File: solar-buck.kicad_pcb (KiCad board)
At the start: 2 copper layers, 51 parts, among them J1 PV_input, J2 Conn_02x19_Odd_Even, J3 Conn_02x19_Odd_Even, J4 Load_output, J5 Batt_output, J6 LED_ON, Q1 PMN30ENEA, Q2 PMN30ENEA, Q3 NX3008PBK, Q4 NX3008PBK, SW1 SW_Push, SW2 SW_Push, SW3 SW_Push, SW4 SW_Push, U1 TS2937, U2 MAX1614, U3 MCP1804, U4 L6285E, U5 MAX4378

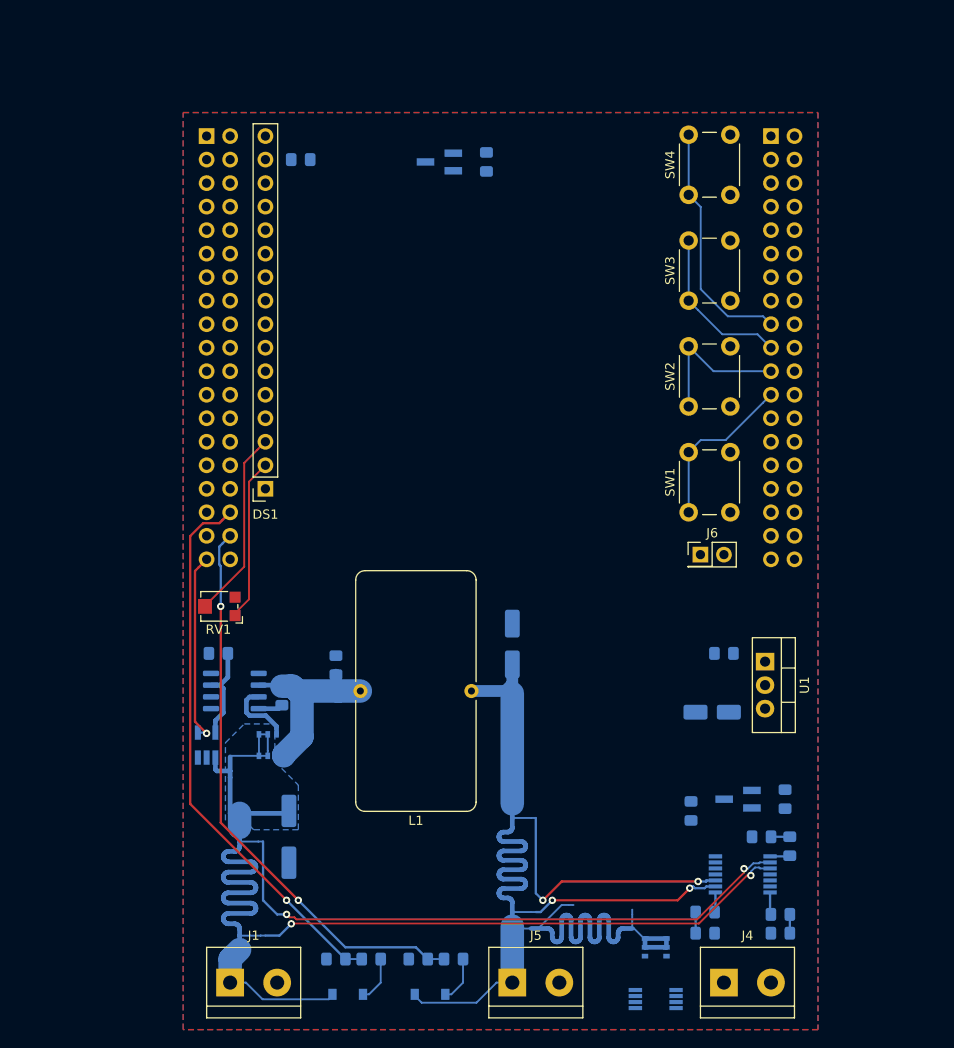
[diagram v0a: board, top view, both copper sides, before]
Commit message: Updated PCB footprints
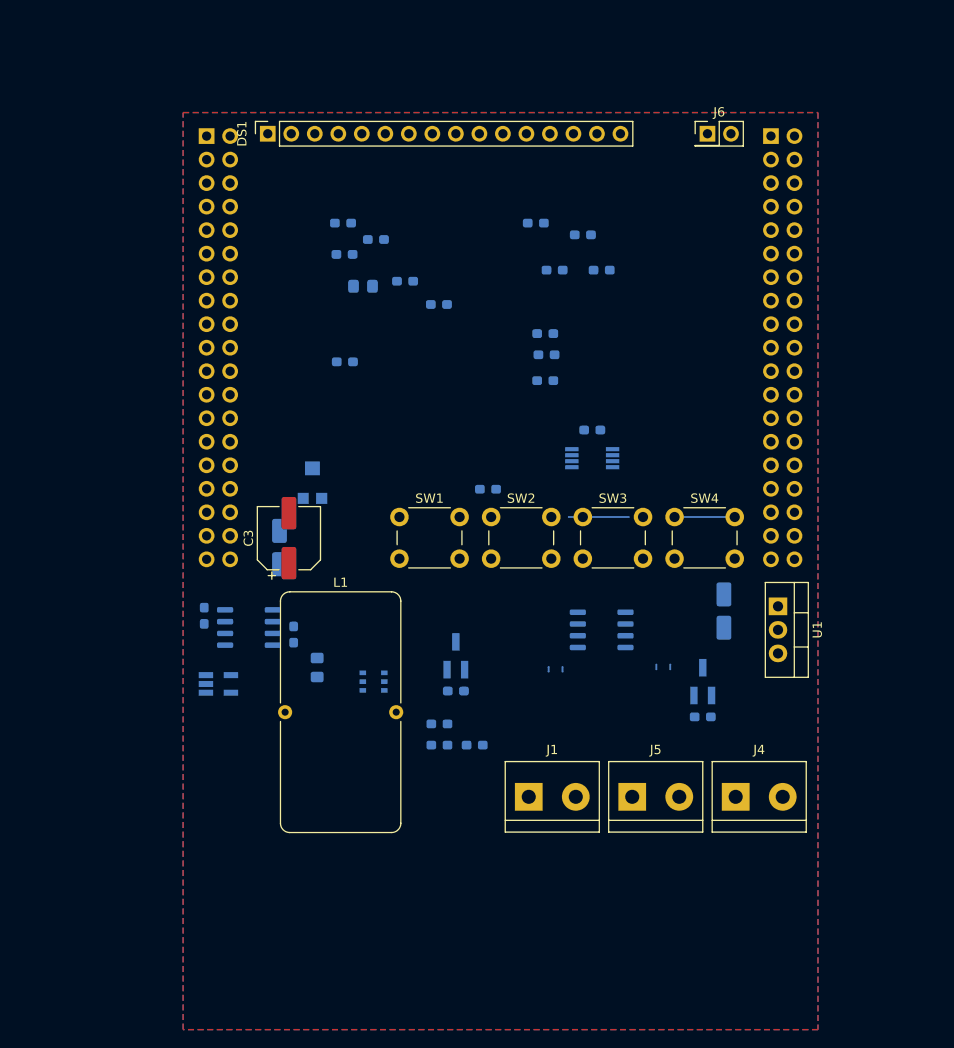
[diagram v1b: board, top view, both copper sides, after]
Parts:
- removed D2: MMSZ5237BT1G, Diode_SMD:D_SOD-123
- removed D3: MMSZ5243BT1G, Diode_SMD:D_SOD-123
- removed NT3, NT4: Net-Tie_2, local:NetTie-2_SMD_Pad8mil
- removed Q1: PMN30ENEA, Package_SO:TSOP-6_1.65x3.05mm_P0.95mm
- added C11: 100n, Capacitor_SMD:C_0603_1608Metric_Pad1.05x0.95mm_HandSolder, B.Cu at (178.3, 69.6)
- added D4: RBR5LAM-30TR, Diode_SMD:D_0805_2012Metric_Pad1.15x1.40mm_HandSolder, B.Cu at (176.9, 74.6)
- added R11: 10k, Resistor_SMD:R_0603_1608Metric_Pad1.05x0.95mm_HandSolder, B.Cu at (181.5, 74.1)
- added R12: 100, Resistor_SMD:R_0603_1608Metric_Pad1.05x0.95mm_HandSolder, B.Cu at (185.2, 124.2)
- added R13: 10k, Resistor_SMD:R_0603_1608Metric_Pad1.05x0.95mm_HandSolder, B.Cu at (185.2, 121.9)
- added R14: 100, Resistor_SMD:R_0603_1608Metric_Pad1.05x0.95mm_HandSolder, B.Cu at (189.0, 124.2)
- C10, C2, C4, C5, C7, C8, C9: footprint Capacitor_SMD:C_0805_2012Metric_Pad1.15x1.40mm_HandSolder -> Capacitor_SMD:C_0603_1608Metric_Pad1.05x0.95mm_HandSolder
- C3: footprint Capacitor_SMD:CP_Elec_6.3x5.4 -> Capacitor_SMD:CP_Elec_6.3x7.7; moved to F.Cu
- C6: footprint Capacitor_SMD:CP_Elec_5x5.4 -> Capacitor_SMD:CP_Elec_4x5.4
- R1, R3: value 10k -> 200k; footprint Resistor_SMD:R_0805_2012Metric_Pad1.15x1.40mm_HandSolder -> Resistor_SMD:R_0603_1608Metric_Pad1.05x0.95mm_HandSolder
- R10: value 100k -> 200k; footprint Resistor_SMD:R_0805_2012Metric_Pad1.15x1.40mm_HandSolder -> Resistor_SMD:R_0603_1608Metric_Pad1.05x0.95mm_HandSolder
- R2: value 200 -> 100; footprint Resistor_SMD:R_0805_2012Metric_Pad1.15x1.40mm_HandSolder -> Resistor_SMD:R_0603_1608Metric_Pad1.05x0.95mm_HandSolder
- R4: value 150k -> 1.8M; footprint Resistor_SMD:R_0805_2012Metric_Pad1.15x1.40mm_HandSolder -> Resistor_SMD:R_0603_1608Metric_Pad1.05x0.95mm_HandSolder
- R5: value 200k -> 1.8M; footprint Resistor_SMD:R_0805_2012Metric_Pad1.15x1.40mm_HandSolder -> Resistor_SMD:R_0603_1608Metric_Pad1.05x0.95mm_HandSolder
- R6, R8: footprint Resistor_SMD:R_0805_2012Metric_Pad1.15x1.40mm_HandSolder -> Resistor_SMD:R_0603_1608Metric_Pad1.05x0.95mm_HandSolder
- R7: value 3.3k -> 10k; footprint Resistor_SMD:R_0805_2012Metric_Pad1.15x1.40mm_HandSolder -> Resistor_SMD:R_0603_1608Metric_Pad1.05x0.95mm_HandSolder
- R9: value 120k -> 200k; footprint Resistor_SMD:R_0805_2012Metric_Pad1.15x1.40mm_HandSolder -> Resistor_SMD:R_0603_1608Metric_Pad1.05x0.95mm_HandSolder
- RV1: moved to B.Cu
- U2: value MAX1614 -> VN5E160MS-E; footprint Package_SO:MSOP-8_3x3mm_P0.65mm -> Package_SO:SO-8_3.9x4.9mm_P1.27mm
- U5: value MAX4378 -> MAX4377; footprint Package_SO:TSSOP-14_4.4x5mm_P0.65mm -> Package_SO:MSOP-8_3x3mm_P0.65mm
- moved R10 79.5 mm to (174.8, 67.8)
- moved R8 76.6 mm to (195.6, 67.8)
- moved R5 76.2 mm to (174.9, 71.2)
- moved R7 75.5 mm to (185.1, 76.6), turned to 0 degrees
- moved C10 73.4 mm to (197.6, 72.9), turned to 0 degrees
- moved R9 68.9 mm to (196.6, 79.8)
- moved C8 67.8 mm to (200.7, 69.1), turned to 0 degrees
- moved R4 66.0 mm to (196.7, 82.0)
- moved R6 65.5 mm to (202.7, 72.9), turned to 0 degrees
- moved C9 64.9 mm to (196.6, 84.8)
- moved R1 57.2 mm to (186.9, 118.4), turned to 0 degrees
- moved Q3 53.4 mm to (186.9, 114.6), turned to 90 degrees
- moved C2 51.7 mm to (175.0, 82.8), turned to 0 degrees
- moved U5 47.8 mm to (201.7, 93.2), turned to 0 degrees
- moved J6 45.5 mm to (214.1, 58.2)
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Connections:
- C10 pad 2: /ADC_load_I -> /ADC_batt_I
- C6 pad 1: /V_batt -> Net-(C6-Pad1)
- C9 pad 2: /ADC_buck_I -> /ADC_batt
- DS1 pad 10: Net-(DS1-Pad10) -> (no net)
- DS1 pad 7: Net-(DS1-Pad7) -> (no net)
- DS1 pad 8: Net-(DS1-Pad8) -> (no net)
- DS1 pad 9: Net-(DS1-Pad9) -> (no net)
- J2 pad 1: Net-(J2-Pad1) -> (no net)
- J2 pad 10: Net-(J2-Pad10) -> (no net)
- J2 pad 11: Net-(J2-Pad11) -> (no net)
- J2 pad 12: Net-(J2-Pad12) -> (no net)
- J2 pad 13: Net-(J2-Pad13) -> (no net)
- J2 pad 14: Net-(J2-Pad14) -> (no net)
- J2 pad 15: Net-(J2-Pad15) -> (no net)
- J2 pad 16: Net-(J2-Pad16) -> (no net)
- J2 pad 17: Net-(J2-Pad17) -> (no net)
- J2 pad 18: Net-(J2-Pad18) -> (no net)
- J2 pad 2: Net-(J2-Pad2) -> (no net)
- J2 pad 21: Net-(J2-Pad21) -> (no net)
- J2 pad 23: /PM_OFF -> /CS_DIS
- J2 pad 24: Net-(J2-Pad24) -> (no net)
- J2 pad 25: /PM_ON -> /LOAD_EN
- J2 pad 26: Net-(J2-Pad26) -> (no net)
- J2 pad 27: /PM_LBO -> (no net)
- J2 pad 29: Net-(J2-Pad29) -> (no net)
- J2 pad 3: Net-(J2-Pad3) -> (no net)
- J2 pad 30: /ADC_buck_I -> /ADC_batt_I
- J2 pad 31: Net-(J2-Pad31) -> (no net)
- J2 pad 33: Net-(J2-Pad33) -> (no net)
- J2 pad 4: Net-(J2-Pad4) -> (no net)
- J2 pad 5: Net-(J2-Pad5) -> (no net)
- J2 pad 7: Net-(J2-Pad7) -> (no net)
- J2 pad 9: Net-(J2-Pad9) -> (no net)
- J3 pad 1: Net-(J3-Pad1) -> (no net)
- J3 pad 10: Net-(J3-Pad10) -> (no net)
- J3 pad 11: Net-(J3-Pad11) -> (no net)
- J3 pad 12: Net-(J3-Pad12) -> (no net)
- J3 pad 13: Net-(J3-Pad13) -> (no net)
- J3 pad 14: Net-(J3-Pad14) -> (no net)
- J3 pad 15: Net-(J3-Pad15) -> (no net)
- J3 pad 16: Net-(J3-Pad16) -> (no net)
- J3 pad 18: Net-(J3-Pad18) -> (no net)
- J3 pad 2: Net-(J3-Pad2) -> (no net)
- J3 pad 22: Net-(J3-Pad22) -> (no net)
- J3 pad 24: Net-(J3-Pad24) -> (no net)
- J3 pad 26: Net-(J3-Pad26) -> (no net)
- J3 pad 28: Net-(J3-Pad28) -> (no net)
- J3 pad 3: Net-(J3-Pad3) -> (no net)
- J3 pad 32: Net-(J3-Pad32) -> (no net)
- J3 pad 35: Net-(J3-Pad35) -> (no net)
- J3 pad 36: Net-(J3-Pad36) -> (no net)
- J3 pad 37: Net-(J3-Pad37) -> (no net)
- J3 pad 38: Net-(J3-Pad38) -> (no net)
- J3 pad 4: Net-(J3-Pad4) -> (no net)
- J3 pad 5: Net-(J3-Pad5) -> (no net)
- J3 pad 6: Net-(J3-Pad6) -> (no net)
- J3 pad 7: Net-(J3-Pad7) -> (no net)
- J3 pad 8: Net-(J3-Pad8) -> (no net)
- L1 pad 2: /V_batt -> Net-(C6-Pad1)
- R3 pad 1: /HSCA_SHDN -> +5V
- R3 pad 2: +5V -> /HSCA_SHDN
- R4 pad 2: Net-(D2-Pad2) -> /V_batt
- R5 pad 2: Net-(D3-Pad2) -> /V_solar
- R7 pad 1: /ADC_buck_I -> Net-(R7-Pad1)
- R7 pad 2: Net-(R7-Pad2) -> /LOAD_EN
- R8 pad 1: /ADC_load_I -> /ADC_batt_I
- U2 pad 1: /PM_ON -> GND
- U2 pad 2: /PM_OFF -> Net-(R7-Pad1)
- U2 pad 3: /PM_LBO -> Net-(R12-Pad1)
- U2 pad 4: /ADC_solar -> Net-(R11-Pad1)
- U2 pad 5: GND -> /V_batt
- U2 pad 6: Net-(Q1-Pad3) -> /V_load
- U4 pad 1: Net-(U4-Pad1) -> (no net)
- U4 pad 5: Net-(U4-Pad5) -> (no net)
- U5 pad 4: Net-(C7-Pad1) -> GND
- U5 pad 5: /V_buck+ -> /V_batt-
- U5 pad 6: /V_buck- -> /V_batt+
- U5 pad 7: Net-(R7-Pad2) -> Net-(R8-Pad2)
- U5 pad 8: Net-(R8-Pad2) -> Net-(C7-Pad1)
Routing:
- net /V_batt: track 124.8 -> 0.00 mm
- net /V_solar: track 81.2 -> 0.00 mm
- net /V_solar-: track 64.8 -> 0.00 mm, vias 2 -> 0
- net /ADC_batt: track 61.8 -> 0.00 mm, vias 2 -> 0
- net /ADC_solar: track 59.8 -> 0.00 mm, vias 1 -> 0
- net /V_solar+: track 57.8 -> 0.00 mm, vias 2 -> 0
- net /V_batt+: track 28.8 -> 0.00 mm, vias 2 -> 0
- net Net-(C4-Pad2): track 21.1 -> 0.00 mm
- net /12V_SHDN: track 20.8 -> 0.00 mm, vias 1 -> 0
- net /V_batt-: track 20.7 -> 0.00 mm, vias 2 -> 0
- net Net-(DS1-Pad3): track 20.5 -> 0.00 mm
- net /BTN_BACK: track 26.4 -> 6.50 mm
- net Net-(DS1-Pad2): track 18.0 -> 0.00 mm
- net /BTN_UP: track 18.0 -> 0.00 mm
- net /BTN_DOWN: track 16.5 -> 0.00 mm
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- removed copper zone on B.Cu, net /V_solar

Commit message: PCB complete
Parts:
- added TP1: TestPoint, TestPoint:TestPoint_Pad_1.5x1.5mm, F.Cu at (186.7, 134.4)
- added TP10: TestPoint, TestPoint:TestPoint_Pad_1.5x1.5mm, F.Cu at (221.2, 125.5)
- added TP11: TestPoint, TestPoint:TestPoint_Pad_1.5x1.5mm, F.Cu at (176.0, 61.2)
- added TP12: TestPoint, TestPoint:TestPoint_Pad_1.5x1.5mm, F.Cu at (176.0, 64.0)
- added TP2: TestPoint, TestPoint:TestPoint_Pad_1.5x1.5mm, F.Cu at (183.9, 134.4)
- added TP3: TestPoint, TestPoint:TestPoint_Pad_1.5x1.5mm, F.Cu at (221.2, 121.9)
- added TP4: TestPoint, TestPoint:TestPoint_Pad_1.5x1.5mm, F.Cu at (176.0, 113.8)
- added TP5: TestPoint, TestPoint:TestPoint_Pad_1.5x1.5mm, F.Cu at (224.8, 121.9)
- added TP6: TestPoint, TestPoint:TestPoint_Pad_1.5x1.5mm, F.Cu at (176.0, 110.5)
- added TP7: TestPoint, TestPoint:TestPoint_Pad_1.5x1.5mm, F.Cu at (183.4, 129.8)
- added TP8: TestPoint, TestPoint:TestPoint_Pad_1.5x1.5mm, F.Cu at (186.2, 129.8)
- added TP9: TestPoint, TestPoint:TestPoint_Pad_1.5x1.5mm, F.Cu at (224.8, 125.5)
- NT1, NT2, NT5, NT6, RV1: moved to F.Cu
- U2, U4: footprint Package_SO:SO-8_3.9x4.9mm_P1.27mm -> Package_SO:SOIC-8_3.9x4.9mm_P1.27mm
- moved R1 61.8 mm to (204.7, 59.2), turned to 270 degrees
- moved R10 60.3 mm to (195.3, 124.5)
- moved Q3 59.4 mm to (208.5, 59.2), turned to 0 degrees
- moved R5 58.7 mm to (195.3, 126.2)
- moved R3 57.0 mm to (204.7, 64.9), turned to 270 degrees
- moved C11 55.7 mm to (195.3, 122.7)
- moved SW4 53.4 mm to (167.1, 68.6), turned to 90 degrees
- moved Q4 52.7 mm to (208.5, 64.9), turned to 0 degrees
- moved C2 52.1 mm to (212.3, 119.1)
- moved DS1 50.5 mm to (217.2, 58.4), turned to 0 degrees
- moved D4 49.3 mm to (175.5, 124.0), turned to 180 degrees
- moved R9 45.3 mm to (204.2, 124.5)
- moved R4 44.8 mm to (204.2, 126.2)
- moved J6 43.7 mm to (170.4, 58.4), turned to 180 degrees
- moved R2 39.6 mm to (214.4, 65.0), turned to 270 degrees
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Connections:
- DS1 pad 10: (no net) -> Net-(DS1-Pad10)
- DS1 pad 7: (no net) -> Net-(DS1-Pad7)
- DS1 pad 8: (no net) -> Net-(DS1-Pad8)
- DS1 pad 9: (no net) -> Net-(DS1-Pad9)
- J2 pad 1: (no net) -> Net-(J2-Pad1)
- J2 pad 10: (no net) -> Net-(J2-Pad10)
- J2 pad 11: (no net) -> Net-(J2-Pad11)
- J2 pad 12: (no net) -> Net-(J2-Pad12)
- J2 pad 13: (no net) -> Net-(J2-Pad13)
- J2 pad 14: (no net) -> Net-(J2-Pad14)
- J2 pad 15: (no net) -> Net-(J2-Pad15)
- J2 pad 16: (no net) -> Net-(J2-Pad16)
- J2 pad 17: (no net) -> Net-(J2-Pad17)
- J2 pad 18: (no net) -> Net-(J2-Pad18)
- J2 pad 2: (no net) -> Net-(J2-Pad2)
- J2 pad 21: (no net) -> Net-(J2-Pad21)
- J2 pad 24: (no net) -> Net-(J2-Pad24)
- J2 pad 26: (no net) -> Net-(J2-Pad26)
- J2 pad 27: (no net) -> Net-(J2-Pad27)
- J2 pad 29: (no net) -> Net-(J2-Pad29)
- J2 pad 3: (no net) -> Net-(J2-Pad3)
- J2 pad 31: (no net) -> Net-(J2-Pad31)
- J2 pad 33: (no net) -> Net-(J2-Pad33)
- J2 pad 4: (no net) -> Net-(J2-Pad4)
- J2 pad 5: (no net) -> Net-(J2-Pad5)
- J2 pad 7: (no net) -> Net-(J2-Pad7)
- J2 pad 9: (no net) -> Net-(J2-Pad9)
- J3 pad 1: (no net) -> Net-(J3-Pad1)
- J3 pad 10: (no net) -> Net-(J3-Pad10)
- J3 pad 11: (no net) -> Net-(J3-Pad11)
- J3 pad 12: (no net) -> Net-(J3-Pad12)
- J3 pad 13: (no net) -> Net-(J3-Pad13)
- J3 pad 14: (no net) -> Net-(J3-Pad14)
- J3 pad 15: (no net) -> Net-(J3-Pad15)
- J3 pad 16: (no net) -> Net-(J3-Pad16)
- J3 pad 18: (no net) -> Net-(J3-Pad18)
- J3 pad 2: (no net) -> Net-(J3-Pad2)
- J3 pad 22: (no net) -> Net-(J3-Pad22)
- J3 pad 24: (no net) -> Net-(J3-Pad24)
- J3 pad 26: (no net) -> Net-(J3-Pad26)
- J3 pad 28: (no net) -> Net-(J3-Pad28)
- J3 pad 3: (no net) -> Net-(J3-Pad3)
- J3 pad 32: (no net) -> Net-(J3-Pad32)
- J3 pad 35: (no net) -> Net-(J3-Pad35)
- J3 pad 36: (no net) -> Net-(J3-Pad36)
- J3 pad 37: (no net) -> Net-(J3-Pad37)
- J3 pad 38: (no net) -> Net-(J3-Pad38)
- J3 pad 4: (no net) -> Net-(J3-Pad4)
- J3 pad 5: (no net) -> Net-(J3-Pad5)
- J3 pad 6: (no net) -> Net-(J3-Pad6)
- J3 pad 7: (no net) -> Net-(J3-Pad7)
- J3 pad 8: (no net) -> Net-(J3-Pad8)
- R4 pad 1: /ADC_batt -> /V_batt
- R4 pad 2: /V_batt -> /ADC_batt
- R5 pad 1: /ADC_solar -> /V_solar
- R5 pad 2: /V_solar -> /ADC_solar
- U4 pad 1: (no net) -> Net-(U4-Pad1)
- U4 pad 5: (no net) -> Net-(U4-Pad5)
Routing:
- net +5V: track 0.00 -> 153.3 mm, vias 0 -> 1
- net /V_solar: track 0.00 -> 108.4 mm, vias 0 -> 6
- net Net-(DS1-Pad2): track 0.00 -> 106.9 mm
- net /V_batt: track 0.00 -> 103.8 mm, vias 0 -> 2
- net /LCD_SHDN: track 0.00 -> 91.6 mm, vias 0 -> 3
- net Net-(DS1-Pad3): track 0.00 -> 89.0 mm
- net /ADC_solar: track 0.00 -> 78.0 mm, vias 0 -> 2
- net /BTN_UP: track 0.00 -> 75.7 mm, vias 0 -> 2
- net /ADC_batt_I: track 0.00 -> 75.5 mm, vias 0 -> 3
- net /PWM_buck: track 0.00 -> 75.5 mm, vias 0 -> 3
- net /ADC_batt: track 0.00 -> 75.4 mm, vias 0 -> 1
- net /V_solar+: track 0.00 -> 73.8 mm, vias 0 -> 1
- net /V_solar-: track 0.00 -> 72.9 mm, vias 0 -> 1
- net /V_batt-: track 0.00 -> 72.9 mm, vias 0 -> 1
- net /V_batt+: track 0.00 -> 72.7 mm, vias 0 -> 1
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- added copper zone on B.Cu, net +5V
- added copper zone on B.Cu, net /V_batt
- added copper zone on B.Cu, net /V_load
- added copper zone on B.Cu, net /V_solar
- added copper zone on B.Cu, net Net-(C4-Pad2)
- added copper zone on B.Cu, net Net-(C6-Pad1)
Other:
- board outline added: 71.1 x 83.8 mm
- net class Default: clearance 0.2 -> 0.2032; trace_width 0.25 -> 0.2032
- rule pad_to_mask_clearance: 0 -> 0.2032
- rule trace_clearance: 0.2 -> 0.2032
- rule trace_min: 0.2 -> 0.2032

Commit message: Final changes
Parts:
- added REF**: MountingHole_3.2mm_M3, MountingHole:MountingHole_3.2mm_M3, F.Cu at (215.9, 55.9)
- added REF**: MountingHole_3.2mm_M3, MountingHole:MountingHole_3.2mm_M3, F.Cu at (184.9, 130.9)
- added REF**: MountingHole_3.2mm_M3, MountingHole:MountingHole_3.2mm_M3, F.Cu at (184.9, 55.9)
- added REF**: MountingHole_3.2mm_M3, MountingHole:MountingHole_3.2mm_M3, F.Cu at (167.6, 54.6)
- added REF**: MountingHole_3.2mm_M3, MountingHole:MountingHole_3.2mm_M3, F.Cu at (200.7, 106.7)
- C3, NT1, NT2, NT5, NT6: moved to B.Cu
- moved TP1 77.7 mm to (177.8, 57.1)
- moved TP2 77.7 mm to (175.0, 57.1)
- moved TP7 75.9 mm to (175.0, 54.4)
- moved TP8 75.9 mm to (177.8, 54.4)
- moved J6 52.1 mm to (222.2, 53.3), turned to 0 degrees
- moved NT6 11.9 mm to (199.9, 129.8)
- moved NT2 9.92 mm to (180.8, 136.9)
- moved NT1 6.37 mm to (188.5, 136.9)
- moved J4 5.36 mm to (217.2, 138.4)
- moved J5 5.34 mm to (205.7, 138.4)
- moved J1 5.33 mm to (194.3, 138.4)
- moved NT5 5.11 mm to (192.3, 129.8)
- moved R2 4.38 mm to (213.6, 69.3)
- moved DS1 3.22 mm to (215.9, 61.4)
- moved C3 1.80 mm to (177.8, 131.6)
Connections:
- TP1 pad 1: /V_solar -> /V_solar+
- TP2 pad 1: /V_solar -> /V_solar-
- TP7 pad 1: /V_batt -> /V_batt+
- TP8 pad 1: /V_batt -> /V_batt-
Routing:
- net /V_solar-: track 72.9 -> 106.3 mm, vias 1 -> 3
- net /V_batt-: track 72.9 -> 105.5 mm, vias 1 -> 3
- net /V_batt+: track 72.7 -> 104.5 mm, vias 1 -> 3
- net /V_solar+: track 73.8 -> 97.8 mm, vias 1 -> 3
- net /6: track 65.8 -> 48.8 mm, vias 2 -> 1
- net /V_batt: track 103.8 -> 91.3 mm, vias 2 -> 0
- net Net-(DS1-Pad2): track 106.9 -> 113.1 mm
- net /V_load: track 25.9 -> 32.0 mm
- net /LCD_EN: track 32.7 -> 28.7 mm
- net GND: track 4.00 -> 7.65 mm, vias 58 -> 59
- net /V_solar: track 108.4 -> 104.9 mm, vias 6 -> 1
- net /LCD_RS: track 34.8 -> 31.7 mm
- net Net-(DS1-Pad3): track 89.0 -> 91.4 mm
- net /LCD_D5: track 9.20 -> 7.01 mm
- net /LCD_D4: track 9.20 -> 7.01 mm
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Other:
- board size 71.1 x 83.8 mm -> 71.1 x 92.7 mm
